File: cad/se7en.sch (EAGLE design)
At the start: 59 parts, among them CN1 MICROSD-EJECT, CN3 DO NOT PLACE, CN4 DO NOT PLACE, SW1 SWITCHKMR211, SW2 SWITCHKMR211, U1 ATSAME70, X1 12MHz, X2 32k768

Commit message: charger
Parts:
- removed D1: 1A, jaw:DIODE-0805
- added LED3: LED, jaw:LED
- added Q1: FDC6329S, jaw:FDC6329S
- added R10: 1M, jaw:R0603
- added R11: 1k, jaw:R-0402
- added R9: 10k, jaw:R0603
- added U2: MCP73831/OT, adafruit:MCP73831/OT
- C1: value 4u7 -> .1u
- C2, C3: value (none) -> .1u
- L1: value 10u -> 1u
- L2, L3: value (none) -> 1u
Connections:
- removed net N$15: D1.A, F1.2
- new net N$10: LED3.C, U2.STAT
- new net N$12: LED3.A, R11.P$1
- new net N$17: R9.P$1, U2.PROG
- new net VIN: F1.2, Q1.A, Q1.G, R10.P$2, R11.P$2, U2.VDD
- new net VSYS: Q1.C, Q1.S, VR1.EN, VR1.VIN
- net GND: now also R10.P$1, R9.P$2, U2.VSS
- net VBAT: now also Q1.D, U2.VBAT; no longer D1.C, VR1.EN, VR1.VIN
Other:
- moved on the sheet: C2, C20, C21, C22, C3, CN2, F1, VR1

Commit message: tweak
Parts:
- added C25: 10u, jaw:C0603
- added CN6, CN7: DO NOT PLACE, jaw:HEADER-1X1SMALL
- C5, C6, C7: device jaw:C0603 -> jaw:C-0402
- CN5: value (none) -> DO NOT PLACE
- L1, L2, L3: value 1u -> FB
- LED1: value LED -> white
- LED3: value LED -> RED
- R1, R10, R2, R3, R9: device jaw:R0603 -> jaw:R-0402
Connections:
- new net PIEZO: CN7.P$1, U1.PA0
- new net PINA12: U1.PA12
- net GND: now also C25.P$2, CN6.P$1
- net VSYS: now also C25.P$1
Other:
- note added: "10k => 100mA charge"
- note added: "battery charger"
- note added: "data sheet recommends L1/C1 filter xplained board does not include"
- note added: "diag/serial"
- note added: "erase button"
- note added: "lights + sounds"
- note added: "load share"
- note added: "micro SD card"
- note added: "piezo"
- note added: "power"
- note added: "reset button"
- note added: "single wire debug"
- note added: "slow clock circuit: optional"
- note added: "voltage regulator"
- moved on the sheet: C24, CN3, CN4, LED1, LED2, R5, R7, R8

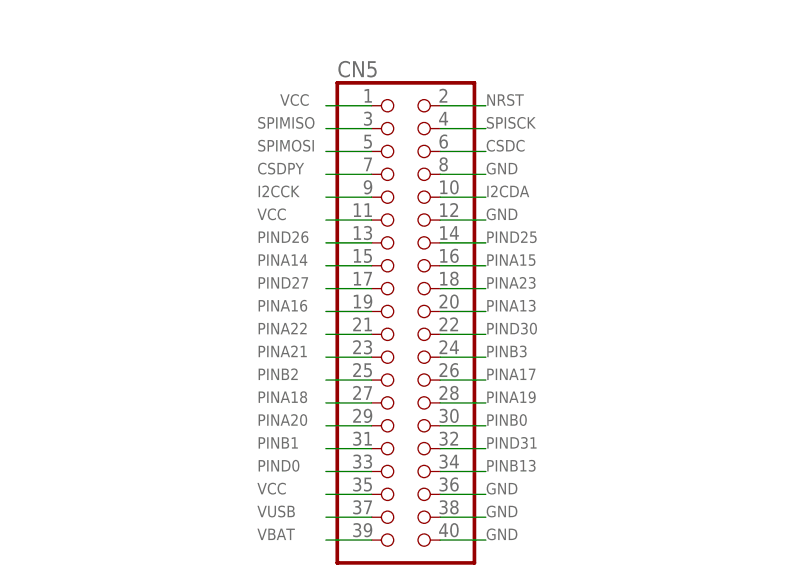
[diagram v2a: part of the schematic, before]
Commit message: replace A22 with A12
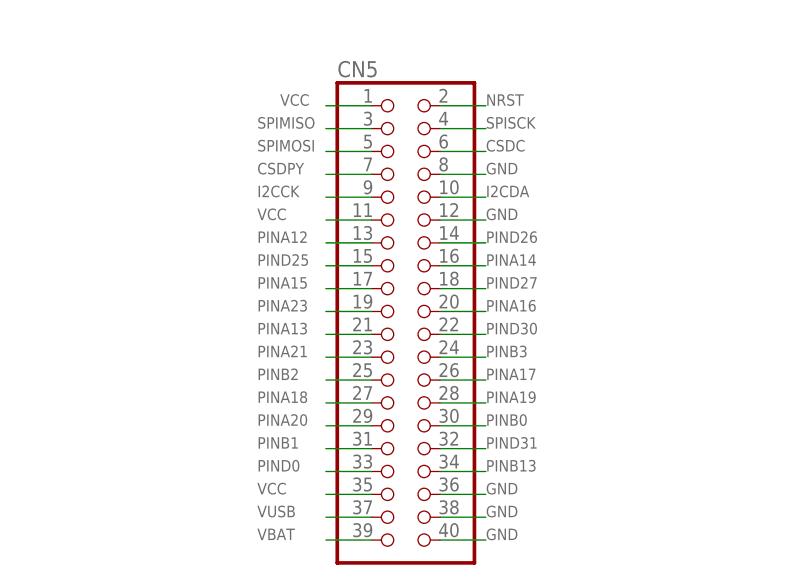
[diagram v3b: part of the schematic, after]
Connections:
- net PINA12: now also CN5.13
- net PINA13: now also CN5.21; no longer CN5.20
- net PINA14: now also CN5.16; no longer CN5.15
- net PINA15: now also CN5.17; no longer CN5.16
- net PINA16: now also CN5.20; no longer CN5.19
- net PINA22: no longer CN5.21
- net PINA23: now also CN5.19; no longer CN5.18
- net PIND25: now also CN5.15; no longer CN5.14
- net PIND26: now also CN5.14; no longer CN5.13
- net PIND27: now also CN5.18; no longer CN5.17
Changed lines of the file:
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@@
+</segment>
+<segment>
+<pinref part="CN5" gate="A" pin="21"/>
+<wire x1="353.06" y1="193.04" x2="347.98" y2="193.04" width="0.1524" layer="91"/>
+<label x="340.36" y="193.04" size="1.27" layer="95"/>
+</segment>
+</net>
+<net name="PINA14" class="0">
+<segment>
+<pinref part="U1" gate="G$1" pin="PA14"/>
+<wire x1="170.18" y1="149.86" x2="165.1" y2="149.86" width="0.1524" layer="91"/>
+<label x="157.48" y="149.86" size="1.27" layer="95"/>
+</segment>
+<segment>
+<pinref part="CN5" gate="A" pin="16"/>
+<wire x1="360.68" y1="200.66" x2="365.76" y2="200.66" width="0.1524" layer="91"/>
+<label x="365.76" y="200.66" size="1.27" layer="95"/>
+</segment>
+</net>
+<net name="PINA15" class="0">
+<segment>
+<pinref part="U1" gate="G$1" pin="PA15"/>
+<wire x1="170.18" y1="147.32" x2="165.1" y2="147.32" width="0.1524" layer="91"/>
+<label x="157.48" y="147.32" size="1.27" layer="95"/>
+</segment>
+<segment>
+<pinref part="CN5" gate="A" pin="17"/>
+<wire x1="353.06" y1="198.12" x2="347.98" y2="198.12" width="0.1524" layer="91"/>
+<label x="340.36" y="198.12" size="1.27" layer="95"/>
+</segment>
+</net>
+<net name="PINA16" class="0">
+<segment>
+<pinref part="U1" gate="G$1" pin="PA16"/>
+<wire x1="170.18" y1="144.78" x2="165.1" y2="144.78" width="0.1524" layer="91"/>
+<label x="157.48" y="144.78" size="1.27" layer="95"/>
 </segment>
 <segment>
@@
 </segment>
 </net>
-<net name="PINA14" class="0">
-<segment>
-<pinref part="U1" gate="G$1" pin="PA14"/>
-<wire x1="170.18" y1="149.86" x2="165.1" y2="149.86" width="0.1524" layer="91"/>
-<label x="157.48" y="149.86" size="1.27" layer="95"/>
+<net name="PINA22" class="0">
+<segment>
+<pinref part="U1" gate="G$1" pin="PA22"/>
+<wire x1="170.18" y1="129.54" x2="165.1" y2="129.54" width="0.1524" layer="91"/>
+<label x="157.48" y="129.54" size="1.27" layer="95"/>
+</segment>
+</net>
+<net name="PINA23" class="0">
+<segment>
+<pinref part="U1" gate="G$1" pin="PA23"/>
+<wire x1="170.18" y1="127" x2="165.1" y2="127" width="0.1524" layer="91"/>
+<label x="157.48" y="127" size="1.27" layer="95"/>
+</segment>
+<segment>
+<pinref part="CN5" gate="A" pin="19"/>
+<wire x1="353.06" y1="195.58" x2="347.98" y2="195.58" width="0.1524" layer="91"/>
+<label x="340.36" y="195.58" size="1.27" layer="95"/>
+</segment>
+</net>
+<net name="PINA24" class="0">
+<segment>
+<pinref part="U1" gate="G$1" pin="PA24"/>
+<wire x1="170.18" y1="124.46" x2="165.1" y2="124.46" width="0.1524" layer="91"/>
+<label x="157.48" y="124.46" size="1.27" layer="95"/>
+</segment>
+</net>
+<net name="PIND24" class="0">
+<segment>
+<pinref part="U1" gate="G$1" pin="PD24"/>
+<wire x1="215.9" y1="101.6" x2="220.98" y2="101.6" width="0.1524" layer="91"/>
+<label x="220.98" y="101.6" size="1.27" layer="95"/>
+</segment>
+</net>
+<net name="PIND25" class="0">
+<segment>
+<pinref part="U1" gate="G$1" pin="PD25"/>
+<wire x1="215.9" y1="99.06" x2="220.98" y2="99.06" width="0.1524" layer="91"/>
+<label x="220.98" y="99.06" size="1.27" layer="95"/>
 </segment>
 <segment>
@@
 </segment>
 </net>
-<net name="PINA15" class="0">
-<segment>
-<pinref part="U1" gate="G$1" pin="PA15"/>
-<wire x1="170.18" y1="147.32" x2="165.1" y2="147.32" width="0.1524" layer="91"/>
-<label x="157.48" y="147.32" size="1.27" layer="95"/>
-</segment>
-<segment>
-<pinref part="CN5" gate="A" pin="16"/>
-<wire x1="360.68" y1="200.66" x2="365.76" y2="200.66" width="0.1524" layer="91"/>
-<label x="365.76" y="200.66" size="1.27" layer="95"/>
-</segment>
-</net>
-<net name="PINA16" class="0">
-<segment>
-<pinref part="U1" gate="G$1" pin="PA16"/>
-<wire x1="170.18" y1="144.78" x2="165.1" y2="144.78" width="0.1524" layer="91"/>
-<label x="157.48" y="144.78" size="1.27" layer="95"/>
-</segment>
-<segment>
-<pinref part="CN5" gate="A" pin="19"/>
-<wire x1="353.06" y1="195.58" x2="347.98" y2="195.58" width="0.1524" layer="91"/>
-<label x="340.36" y="195.58" size="1.27" layer="95"/>
-</segment>
-</net>
-<net name="PINA22" class="0">
-<segment>
-<pinref part="U1" gate="G$1" pin="PA22"/>
-<wire x1="170.18" y1="129.54" x2="165.1" y2="129.54" width="0.1524" layer="91"/>
-<label x="157.48" y="129.54" size="1.27" layer="95"/>
-</segment>
-<segment>
-<pinref part="CN5" gate="A" pin="21"/>
-<wire x1="353.06" y1="193.04" x2="347.98" y2="193.04" width="0.1524" layer="91"/>
-<label x="340.36" y="193.04" size="1.27" layer="95"/>
-</segment>
-</net>
-<net name="PINA23" class="0">
-<segment>
-<pinref part="U1" gate="G$1" pin="PA23"/>
-<wire x1="170.18" y1="127" x2="165.1" y2="127" width="0.1524" layer="91"/>
-<label x="157.48" y="127" size="1.27" layer="95"/>
+<net name="PIND26" class="0">
+<segment>
+<pinref part="U1" gate="G$1" pin="PD26"/>
+<wire x1="215.9" y1="96.52" x2="220.98" y2="96.52" width="0.1524" layer="91"/>
+<label x="220.98" y="96.52" size="1.27" layer="95"/>
+</segment>
+<segment>
+<pinref part="CN5" gate="A" pin="14"/>
+<wire x1="360.68" y1="203.2" x2="365.76" y2="203.2" width="0.1524" layer="91"/>
+<label x="365.76" y="203.2" size="1.27" layer="95"/>
+</segment>
+</net>
+<net name="PIND27" class="0">
+<segment>
+<pinref part="U1" gate="G$1" pin="PD27"/>
+<wire x1="215.9" y1="93.98" x2="220.98" y2="93.98" width="0.1524" layer="91"/>
+<label x="220.98" y="93.98" size="1.27" layer="95"/>
 </segment>
 <segment>
@@
 <wire x1="360.68" y1="198.12" x2="365.76" y2="198.12" width="0.1524" layer="91"/>
 <label x="365.76" y="198.12" size="1.27" layer="95"/>
-</segment>
-</net>
-<net name="PINA24" class="0">
-<segment>
-<pinref part="U1" gate="G$1" pin="PA24"/>
-<wire x1="170.18" y1="124.46" x2="165.1" y2="124.46" width="0.1524" layer="91"/>
-<label x="157.48" y="124.46" size="1.27" layer="95"/>
-</segment>
-</net>
-<net name="PIND24" class="0">
-<segment>
-<pinref part="U1" gate="G$1" pin="PD24"/>
-<wire x1="215.9" y1="101.6" x2="220.98" y2="101.6" width="0.1524" layer="91"/>
-<label x="220.98" y="101.6" size="1.27" layer="95"/>
-</segment>
-</net>
-<net name="PIND25" class="0">
-<segment>
-<pinref part="U1" gate="G$1" pin="PD25"/>
-<wire x1="215.9" y1="99.06" x2="220.98" y2="99.06" width="0.1524" layer="91"/>
-<label x="220.98" y="99.06" size="1.27" layer="95"/>
-</segment>
-<segment>
-<pinref part="CN5" gate="A" pin="14"/>
-<wire x1="360.68" y1="203.2" x2="365.76" y2="203.2" width="0.1524" layer="91"/>
-<label x="365.76" y="203.2" size="1.27" layer="95"/>
-</segment>
-</net>
-<net name="PIND26" class="0">
-<segment>
-<pinref part="U1" gate="G$1" pin="PD26"/>
-<wire x1="215.9" y1="96.52" x2="220.98" y2="96.52" width="0.1524" layer="91"/>
-<label x="220.98" y="96.52" size="1.27" layer="95"/>
-</segment>
-<segment>
-<pinref part="CN5" gate="A" pin="13"/>
-<wire x1="353.06" y1="203.2" x2="347.98" y2="203.2" width="0.1524" layer="91"/>
-<label x="340.36" y="203.2" size="1.27" layer="95"/>
-</segment>
-</net>
-<net name="PIND27" class="0">
-<segment>
-<pinref part="U1" gate="G$1" pin="PD27"/>
-<wire x1="215.9" y1="93.98" x2="220.98" y2="93.98" width="0.1524" layer="91"/>
-<label x="220.98" y="93.98" size="1.27" layer="95"/>
-</segment>
-<segment>
-<pinref part="CN5" gate="A" pin="17"/>
-<wire x1="353.06" y1="198.12" x2="347.98" y2="198.12" width="0.1524" layer="91"/>
-<label x="340.36" y="198.12" size="1.27" layer="95"/>
 </segment>
 </net>
@@
 <wire x1="170.18" y1="154.94" x2="165.1" y2="154.94" width="0.1524" layer="91"/>
 </segment>
-</net>
+<segment>
+<pinref part="CN5" gate="A" pin="13"/>
+<wire x1="353.06" y1="203.2" x2="347.98" y2="203.2" width="0.1524" layer="91"/>
+<label x="340.36" y="203.2" size="1.27" layer="95"/>
+</segment>
+</net>

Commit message: tweak
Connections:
- removed net PINA22: U1.PA22
- net N$10: now also R11.P$1; no longer LED3.C
- net N$12: now also LED3.C, R11.P$2; no longer LED3.A, R11.P$1
- net VIN: now also LED3.A; no longer R11.P$2
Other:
- moved on the sheet: LED3, R11
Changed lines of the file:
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@@
 <instance part="GND19" gate="G$1" x="68.58" y="45.72"/>
 <instance part="GND20" gate="G$1" x="106.68" y="68.58"/>
-<instance part="LED3" gate="G$1" x="25.4" y="50.8"/>
-<instance part="R11" gate="G$1" x="17.78" y="55.88" rot="R90"/>
+<instance part="LED3" gate="G$1" x="17.78" y="55.88" rot="R270"/>
+<instance part="R11" gate="G$1" x="25.4" y="50.8" rot="R180"/>
 <instance part="CN6" gate="G$1" x="43.18" y="132.08"/>
 <instance part="CN7" gate="G$1" x="53.34" y="132.08" rot="R180"/>
@@
 </segment>
 </net>
-<net name="PINA22" class="0">
-<segment>
-<pinref part="U1" gate="G$1" pin="PA22"/>
-<wire x1="170.18" y1="129.54" x2="165.1" y2="129.54" width="0.1524" layer="91"/>
-<label x="157.48" y="129.54" size="1.27" layer="95"/>
-</segment>
-</net>
 <net name="PINA23" class="0">
 <segment>
@@
 <wire x1="27.94" y1="71.12" x2="30.48" y2="71.12" width="0.1524" layer="91"/>
 <junction x="30.48" y="71.12"/>
-<pinref part="R11" gate="G$1" pin="P$2"/>
+<pinref part="LED3" gate="G$1" pin="A"/>
 <wire x1="17.78" y1="60.96" x2="30.48" y2="60.96" width="0.1524" layer="91"/>
 <junction x="30.48" y="60.96"/>
-</segment>
-</net>
-<net name="N$10" class="0">
-<segment>
-<pinref part="U2" gate="G$1" pin="STAT"/>
-<pinref part="LED3" gate="G$1" pin="C"/>
-</segment>
-</net>
-<net name="N$12" class="0">
-<segment>
-<pinref part="LED3" gate="G$1" pin="A"/>
-<pinref part="R11" gate="G$1" pin="P$1"/>
-<wire x1="17.78" y1="50.8" x2="20.32" y2="50.8" width="0.1524" layer="91"/>
 </segment>
 </net>
@@
 </segment>
 </net>
+<net name="N$10" class="0">
+<segment>
+<pinref part="U2" gate="G$1" pin="STAT"/>
+<pinref part="R11" gate="G$1" pin="P$1"/>
+</segment>
+</net>
+<net name="N$12" class="0">
+<segment>
+<pinref part="R11" gate="G$1" pin="P$2"/>
+<pinref part="LED3" gate="G$1" pin="C"/>
+<wire x1="20.32" y1="50.8" x2="17.78" y2="50.8" width="0.1524" layer="91"/>
+</segment>
+</net>

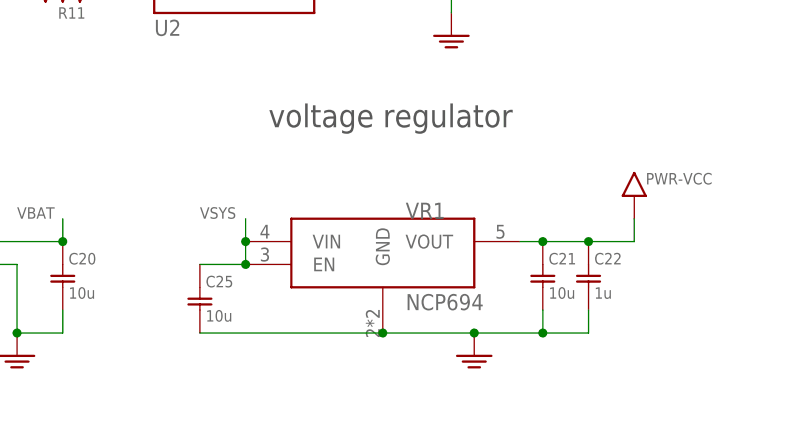
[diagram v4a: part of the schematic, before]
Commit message: smaller/cheaper regulator
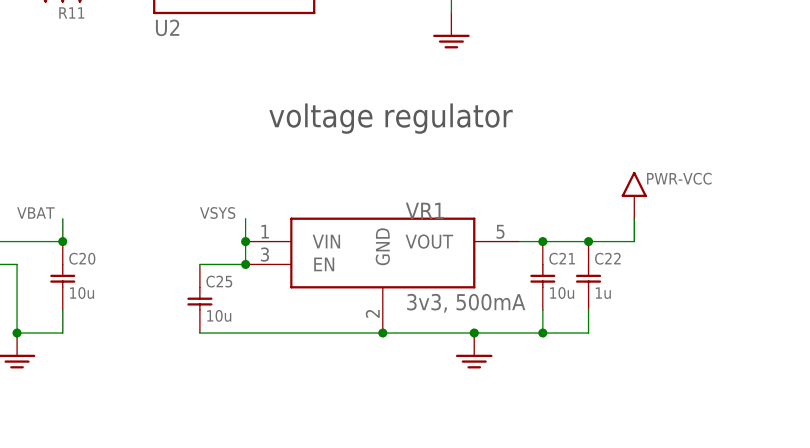
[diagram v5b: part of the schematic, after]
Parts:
- VR1: value NCP694 -> 3v3, 500mA; device jaw:NCP694 -> jaw:REGULATOR4-SOT23
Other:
- moved on the sheet: VR1
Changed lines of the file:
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@@
 <part name="LOGO1" library="SparkFun-Aesthetics" deviceset="OSHW-LOGO" device="M"/>
 <part name="U2" library="adafruit" deviceset="MCP73831" device="/OT"/>
-<part name="VR1" library="jaw" deviceset="NCP694" device=""/>
+<part name="VR1" library="jaw" deviceset="REGULATOR4" device="-SOT23" value="3v3, 500mA"/>
 <part name="R7" library="jaw" deviceset="R" device="-0402" value="1k"/>
 <part name="R8" library="jaw" deviceset="R" device="-0402" value="1k"/>

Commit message: tweak
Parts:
- U2: value MCP73831/OT -> MCP73831; device adafruit:MCP73831/OT -> jaw:MCP73831
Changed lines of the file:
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@@
 <grid distance="0.1" unitdist="inch" unit="inch" style="lines" multiple="1" display="no" altdistance="0.01" altunitdist="inch" altunit="inch"/>
 <layers>
-<layer number="1" name="Top" color="4" fill="1" visible="yes" active="no"/>
-<layer number="2" name="Route2" color="6" fill="1" visible="yes" active="no"/>
-<layer number="3" name="Route3" color="4" fill="3" visible="yes" active="no"/>
-<layer number="14" name="Route14" color="1" fill="6" visible="yes" active="no"/>
-<layer number="15" name="Route15" color="13" fill="1" visible="yes" active="no"/>
-<layer number="16" name="Bottom" color="1" fill="1" visible="yes" active="no"/>
-<layer number="17" name="Pads" color="2" fill="1" visible="yes" active="no"/>
-<layer number="18" name="Vias" color="2" fill="1" visible="yes" active="no"/>
-<layer number="19" name="Unrouted" color="6" fill="1" visible="yes" active="no"/>
-<layer number="20" name="Dimension" color="15" fill="1" visible="yes" active="no"/>
-<layer number="21" name="tPlace" color="7" fill="1" visible="yes" active="no"/>
-<layer number="22" name="bPlace" color="7" fill="1" visible="yes" active="no"/>
-<layer number="23" name="tOrigins" color="15" fill="1" visible="yes" active="no"/>
-<layer number="24" name="bOrigins" color="15" fill="1" visible="yes" active="no"/>
-<layer number="25" name="tNames" color="7" fill="1" visible="yes" active="no"/>
-<layer number="26" name="bNames" color="7" fill="1" visible="yes" active="no"/>
-<layer number="27" name="tValues" color="7" fill="1" visible="yes" active="no"/>
-<layer number="28" name="bValues" color="7" fill="1" visible="yes" active="no"/>
+<layer number="1" name="Top" color="4" fill="1" visible="no" active="no"/>
+<layer number="2" name="Route2" color="6" fill="1" visible="no" active="no"/>
+<layer number="3" name="Route3" color="4" fill="3" visible="no" active="no"/>
+<layer number="14" name="Route14" color="1" fill="6" visible="no" active="no"/>
+<layer number="15" name="Route15" color="13" fill="1" visible="no" active="no"/>
+<layer number="16" name="Bottom" color="1" fill="1" visible="no" active="no"/>
+<layer number="17" name="Pads" color="2" fill="1" visible="no" active="no"/>
+<layer number="18" name="Vias" color="2" fill="1" visible="no" active="no"/>
+<layer number="19" name="Unrouted" color="6" fill="1" visible="no" active="no"/>
+<layer number="20" name="Dimension" color="15" fill="1" visible="no" active="no"/>
+<layer number="21" name="tPlace" color="7" fill="1" visible="no" active="no"/>
+<layer number="22" name="bPlace" color="7" fill="1" visible="no" active="no"/>
+<layer number="23" name="tOrigins" color="15" fill="1" visible="no" active="no"/>
+<layer number="24" name="bOrigins" color="15" fill="1" visible="no" active="no"/>
+<layer number="25" name="tNames" color="7" fill="1" visible="no" active="no"/>
+<layer number="26" name="bNames" color="7" fill="1" visible="no" active="no"/>
+<layer number="27" name="tValues" color="7" fill="1" visible="no" active="no"/>
+<layer number="28" name="bValues" color="7" fill="1" visible="no" active="no"/>
 <layer number="29" name="tStop" color="7" fill="3" visible="no" active="no"/>
 <layer number="30" name="bStop" color="7" fill="6" visible="no" active="no"/>
@@
 <layer number="35" name="tGlue" color="7" fill="4" visible="no" active="no"/>
 <layer number="36" name="bGlue" color="7" fill="5" visible="no" active="no"/>
-<layer number="37" name="tTest" color="7" fill="1" visible="yes" active="no"/>
-<layer number="38" name="bTest" color="7" fill="1" visible="yes" active="no"/>
+<layer number="37" name="tTest" color="7" fill="1" visible="no" active="no"/>
+<layer number="38" name="bTest" color="7" fill="1" visible="no" active="no"/>
 <layer number="39" name="tKeepout" color="4" fill="11" visible="no" active="no"/>
 <layer number="40" name="bKeepout" color="1" fill="11" visible="no" active="no"/>
@@
 <layer number="44" name="Drills" color="7" fill="1" visible="no" active="no"/>
 <layer number="45" name="Holes" color="7" fill="1" visible="no" active="no"/>
-<layer number="46" name="Milling" color="3" fill="1" visible="yes" active="no"/>
-<layer number="47" name="Measures" color="7" fill="1" visible="yes" active="no"/>
-<layer number="48" name="Document" color="7" fill="1" visible="yes" active="no"/>
-<layer number="49" name="Reference" color="7" fill="1" visible="yes" active="no"/>
-<layer number="50" name="dxf" color="7" fill="1" visible="yes" active="no"/>
-<layer number="51" name="tDocu" color="7" fill="1" visible="yes" active="no"/>
-<layer number="52" name="bDocu" color="7" fill="1" visible="yes" active="no"/>
-<layer number="53" name="tGND_GNDA" color="7" fill="1" visible="yes" active="no"/>
-<layer number="54" name="bGND_GNDA" color="7" fill="1" visible="yes" active="no"/>
-<layer number="56" name="wert" color="7" fill="1" visible="yes" active="no"/>
-<layer number="57" name="tCAD" color="7" fill="1" visible="yes" active="no"/>
-<layer number="59" name="tCarbon" color="7" fill="1" visible="yes" active="no"/>
-<layer number="60" name="bCarbon" color="7" fill="1" visible="yes" active="no"/>
+<layer number="46" name="Milling" color="3" fill="1" visible="no" active="no"/>
+<layer number="47" name="Measures" color="7" fill="1" visible="no" active="no"/>
+<layer number="48" name="Document" color="7" fill="1" visible="no" active="no"/>
+<layer number="49" name="Reference" color="7" fill="1" visible="no" active="no"/>
+<layer number="50" name="dxf" color="7" fill="1" visible="no" active="no"/>
+<layer number="51" name="tDocu" color="7" fill="1" visible="no" active="no"/>
+<layer number="52" name="bDocu" color="7" fill="1" visible="no" active="no"/>
+<layer number="53" name="tGND_GNDA" color="7" fill="1" visible="no" active="no"/>
+<layer number="54" name="bGND_GNDA" color="7" fill="1" visible="no" active="no"/>
+<layer number="56" name="wert" color="7" fill="1" visible="no" active="no"/>
+<layer number="57" name="tCAD" color="7" fill="1" visible="no" active="no"/>
+<layer number="59" name="tCarbon" color="7" fill="1" visible="no" active="no"/>
+<layer number="60" name="bCarbon" color="7" fill="1" visible="no" active="no"/>
 <layer number="90" name="Modules" color="5" fill="1" visible="yes" active="yes"/>
 <layer number="91" name="Nets" color="2" fill="1" visible="yes" active="yes"/>
@@
 <part name="U$3" library="jaw" deviceset="ROBOTMAN-LOGO" device="2"/>
 <part name="LOGO1" library="SparkFun-Aesthetics" deviceset="OSHW-LOGO" device="M"/>
-<part name="U2" library="adafruit" deviceset="MCP73831" device="/OT"/>
+<part name="U2" library="jaw" deviceset="MCP73831" device=""/>
 <part name="VR1" library="jaw" deviceset="REGULATOR4" device="-SOT23" value="3v3, 500mA"/>
 <part name="R7" library="jaw" deviceset="R" device="-0402" value="1k"/>
